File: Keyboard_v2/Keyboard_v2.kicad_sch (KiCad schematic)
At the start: 162 parts, among them U1 ProMicro

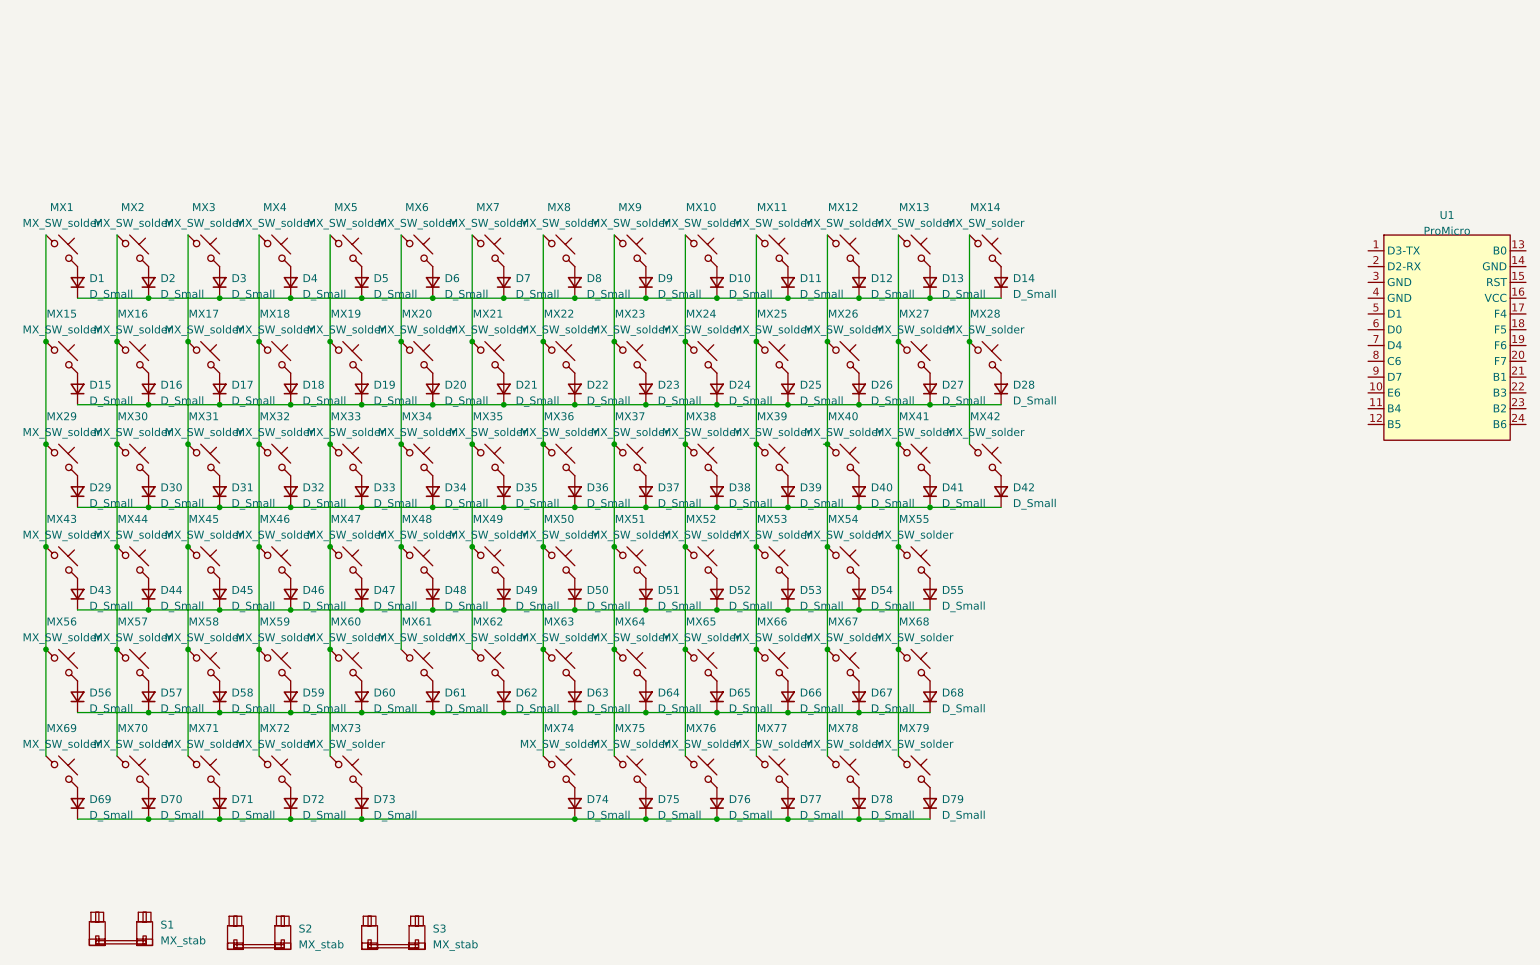
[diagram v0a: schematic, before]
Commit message: all keys routed
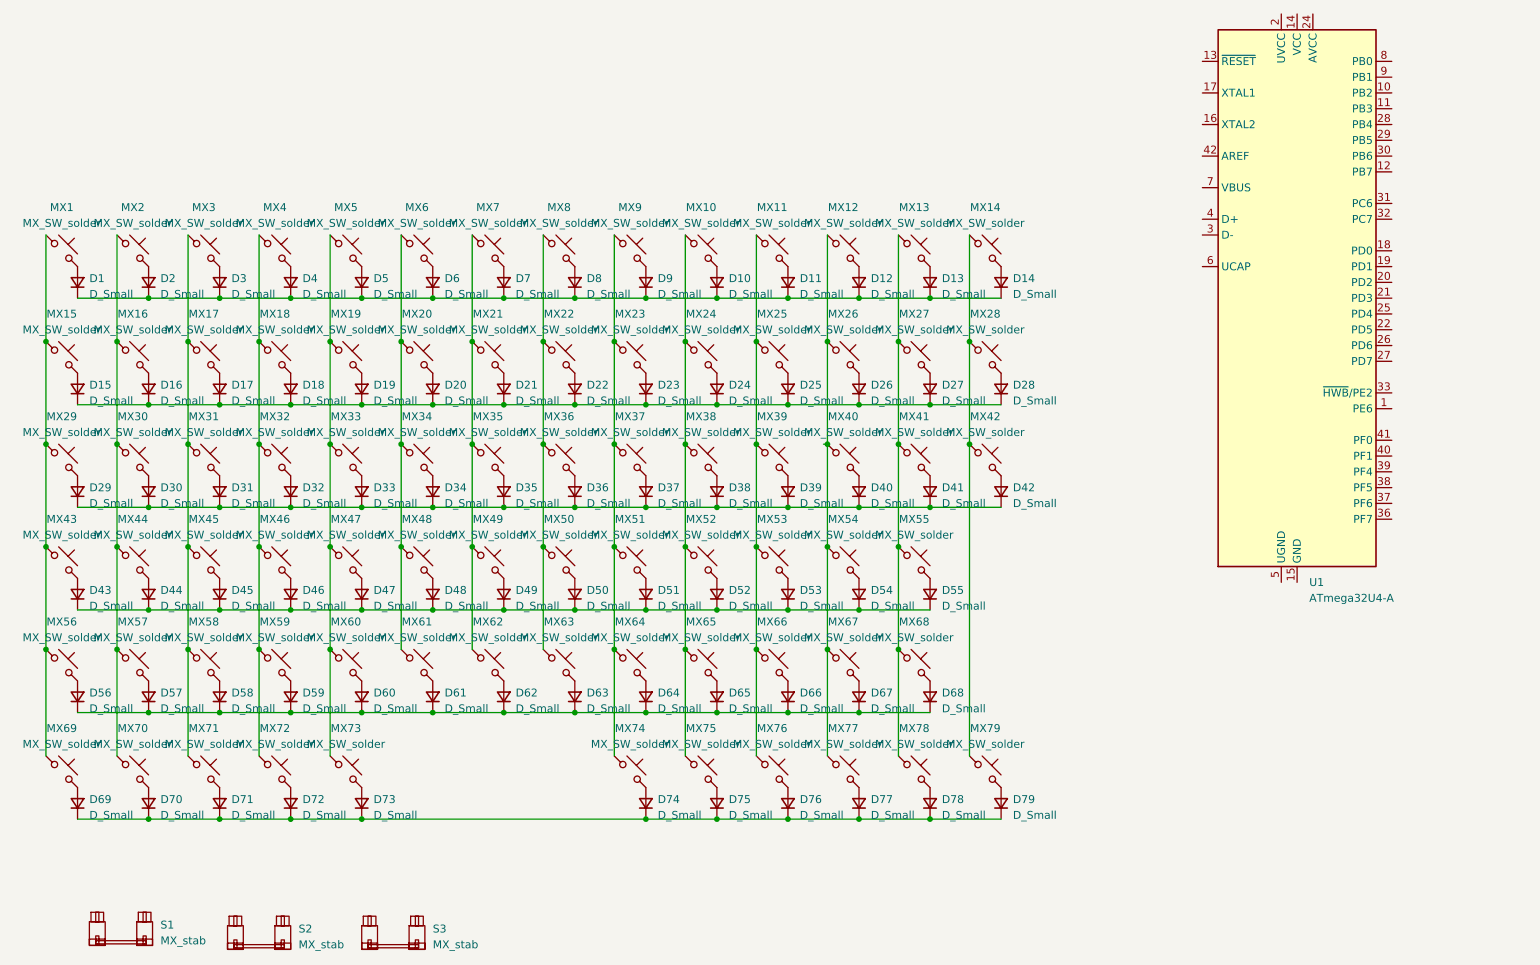
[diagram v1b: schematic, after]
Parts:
- removed U1: ProMicro, PCM_marbastlib-xp-promicroish:ProMicro_USBup, symbol PCM_marbastlib-promicroish:Arduino_ProMicro
- added U1: ATmega32U4-A, Package_QFP:TQFP-44_10x10mm_P0.8mm, symbol MCU_Microchip_ATmega:ATmega32U4-A
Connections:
- net at MX10.1, MX24.1, MX38.1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: now also MX75.1; no longer MX76.1
- net at MX23.1, MX37.1, MX51.1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: now also MX74.1; no longer MX75.1
- net at MX13.1, MX27.1, MX41.1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: now also MX78.1; no longer MX79.1
- net at MX22.1, MX36.1, MX50.1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: no longer MX74.1
- net at MX11.1, MX25.1, MX39.1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: now also MX76.1; no longer MX77.1
- net at MX14.1, MX28.1, MX42.1: now also MX79.1
- net at MX12.1, MX26.1, MX40.1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: now also MX77.1; no longer MX78.1
- new net: U1.14 (VCC), U1.34 (VCC)
- new net: U1.15 (GND), U1.23 (GND), U1.35 (GND), U1.43 (GND)
- new net: U1.24 (AVCC), U1.44 (AVCC)
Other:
- moved on the sheet: D74, D75, D76, D77, D78, D79, MX74, MX75, MX76, MX77, MX78, MX79
